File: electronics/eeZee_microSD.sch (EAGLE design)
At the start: 14 parts, among them U1 MCP1824S, U2 74HC4050, U3 USD-SOCKET

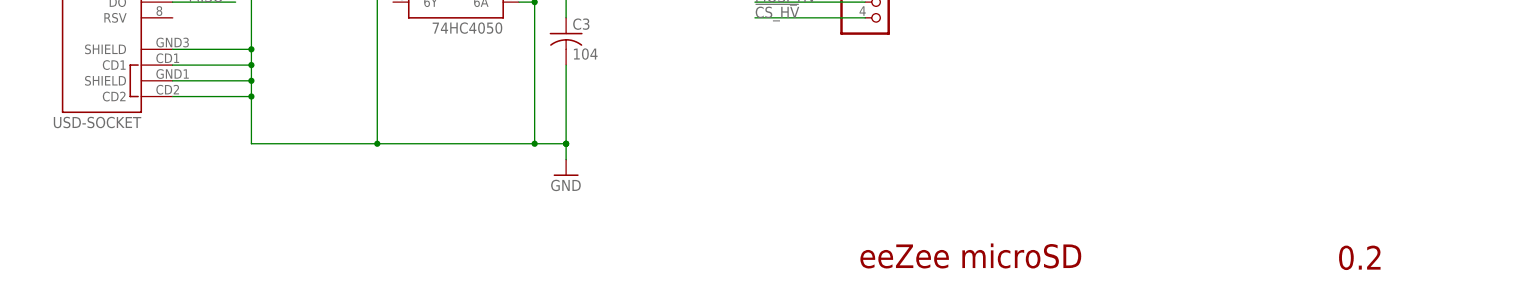
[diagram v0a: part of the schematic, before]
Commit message: Updated schematic version and usd socket value
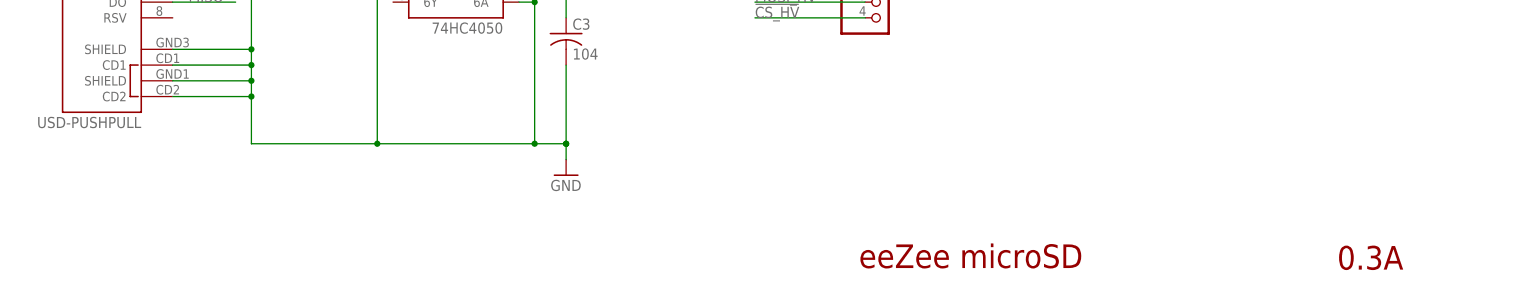
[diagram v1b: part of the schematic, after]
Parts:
- U3: value USD-SOCKET -> USD-PUSHPULL
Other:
- note added: "0.3A"
- note removed: "0.2"
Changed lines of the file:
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@@
 <part name="JP5" library="mes_electromech" deviceset="PINHEAD-2" device="BIG" value="PWR"/>
 <part name="JP4" library="mes_electromech" deviceset="PINHEAD-2" device="BIG" value="PWR"/>
-<part name="U3" library="SparkFun-Connectors" deviceset="USD-SOCKET" device=""/>
+<part name="U3" library="SparkFun-Connectors" deviceset="USD-SOCKET" device="" value="USD-PUSHPULL"/>
 </parts>
 <sheets>
@@
 <text x="181.864" y="143.51" size="1.778" layer="97">to bypass regulator and send VCC direct to the microSD</text>
 <text x="153.924" y="23.114" size="3.81" layer="94">eeZee microSD</text>
-<text x="231.14" y="22.86" size="3.81" layer="94">0.2</text>
+<text x="231.14" y="22.86" size="3.81" layer="94">0.3A</text>
 </plain>
 <instances>

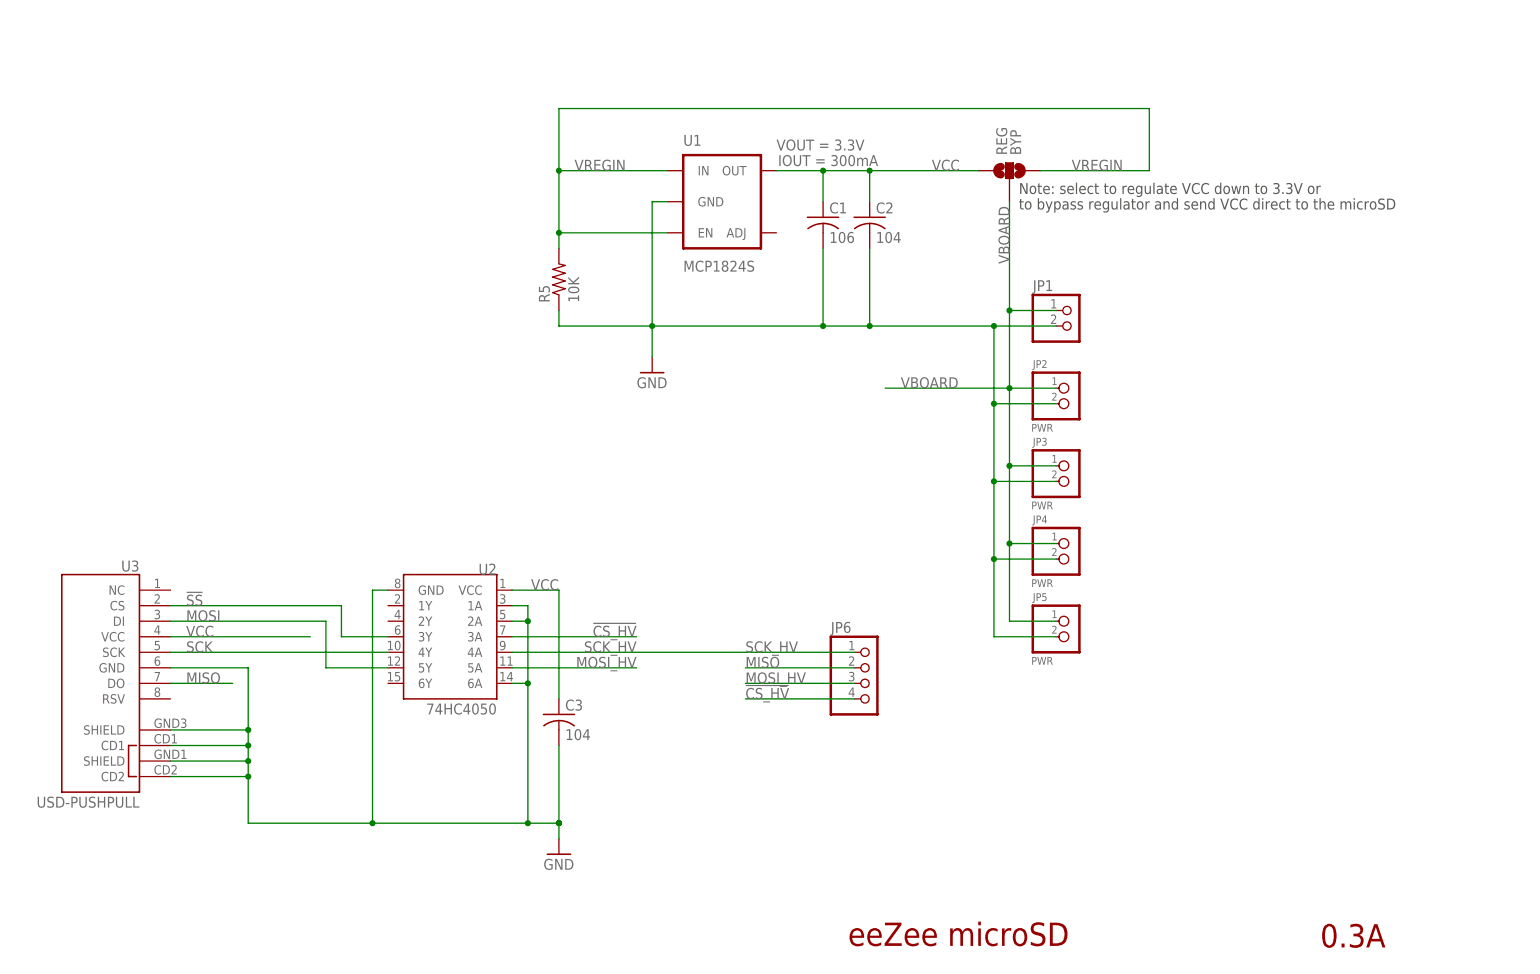
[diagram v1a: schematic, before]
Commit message: Updated version with flip-top socket
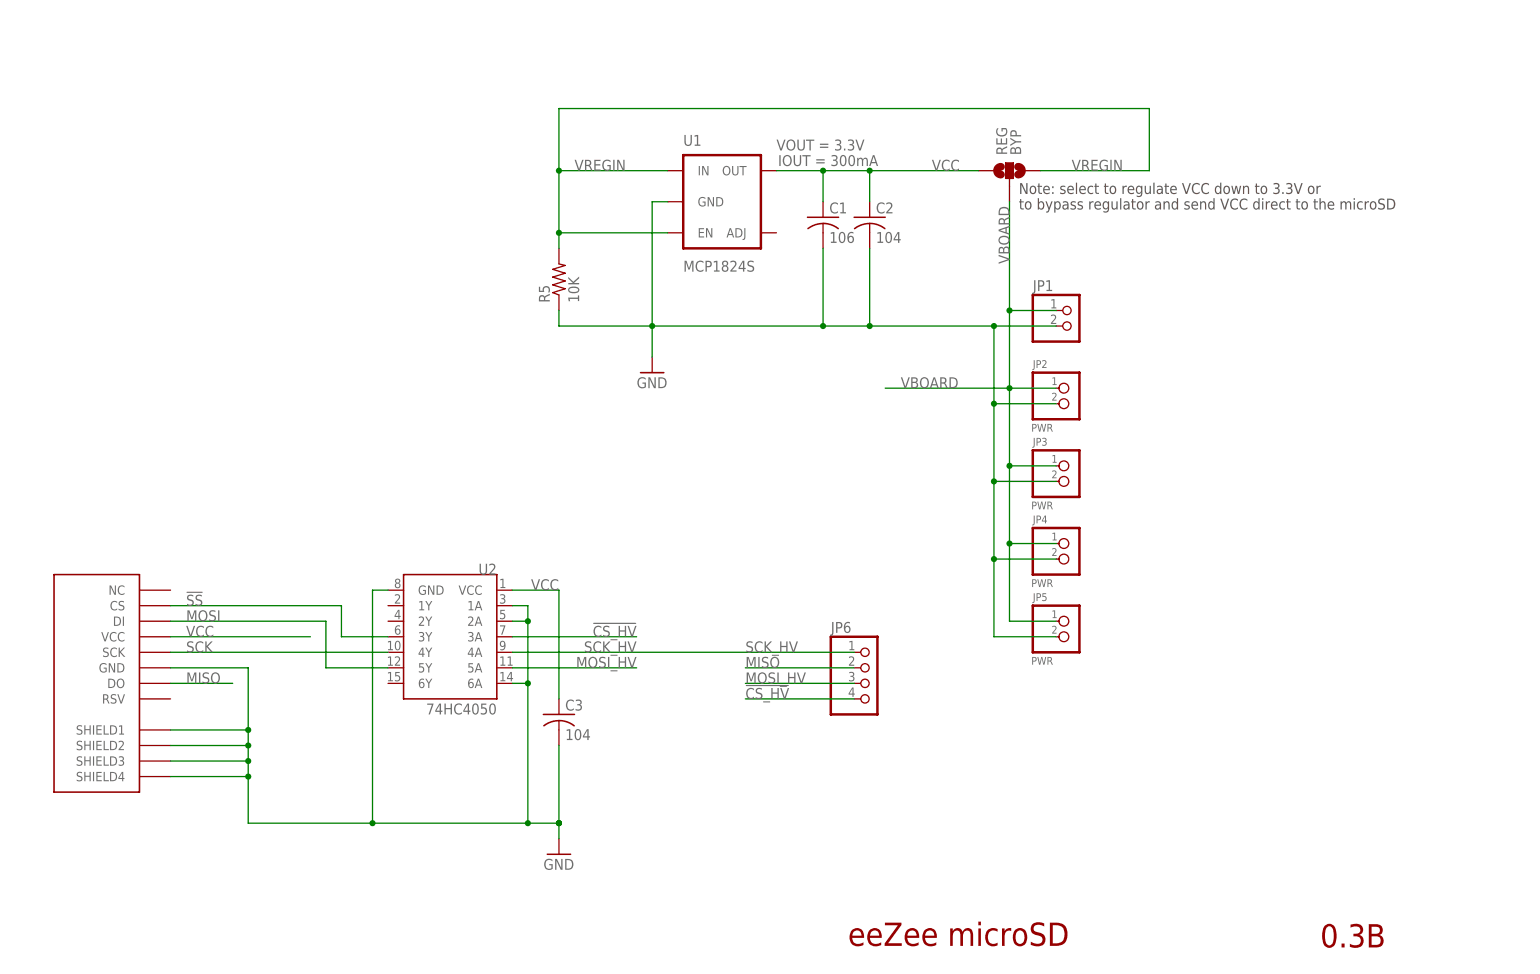
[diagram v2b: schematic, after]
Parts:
- removed U3: USD-PUSHPULL, SparkFun-Connectors:USD-SOCKET
- added U$1: MICROSD_TFLASH, bt_electromech:MICROSD_TFLASH
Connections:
- net !SS: now also U$1.CS; no longer U3.CS
- net GND: now also U$1.GND, U$1.SHIELD1, U$1.SHIELD2, U$1.SHIELD3, U$1.SHIELD4; no longer U3.CD1, U3.CD2, U3.GND, U3.SHIELD@1, U3.SHIELD@3
- net MISO: now also U$1.DO; no longer U3.DO
- net MOSI: now also U$1.DI; no longer U3.DI
- net SCK: now also U$1.SCK; no longer U3.SCK
- net VCC: now also U$1.VCC; no longer U3.VCC
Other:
- note added: "0.3B"
- note removed: "0.3A"
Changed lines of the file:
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@@
 <layer number="49" name="Reference" color="7" fill="1" visible="yes" active="no"/>
 <layer number="50" name="dxf" color="7" fill="1" visible="yes" active="no"/>
-<layer number="51" name="tDocu" color="11" fill="1" visible="yes" active="no"/>
+<layer number="51" name="tDocu" color="15" fill="1" visible="yes" active="no"/>
 <layer number="52" name="bDocu" color="7" fill="1" visible="yes" active="no"/>
 <layer number="53" name="tGND_GNDA" color="7" fill="9" visible="yes" active="no"/>
@@
 <part name="JP5" library="mes_electromech" deviceset="PINHEAD-2" device="BIG" value="PWR"/>
 <part name="JP4" library="mes_electromech" deviceset="PINHEAD-2" device="BIG" value="PWR"/>
-<part name="U3" library="SparkFun-Connectors" deviceset="USD-SOCKET" device="" value="USD-PUSHPULL"/>
+<part name="U$1" library="bt_electromech" deviceset="MICROSD" device="_TFLASH"/>
 </parts>
 <sheets>
@@
 <text x="181.864" y="143.51" size="1.778" layer="97">to bypass regulator and send VCC direct to the microSD</text>
 <text x="153.924" y="23.114" size="3.81" layer="94">eeZee microSD</text>
-<text x="231.14" y="22.86" size="3.81" layer="94">0.3A</text>
+<text x="231.14" y="22.86" size="3.81" layer="94">0.3B</text>
 </plain>
 <instances>
@@
 <instance part="JP5" gate="JP1" x="190.5" y="73.66"/>
 <instance part="JP4" gate="JP1" x="190.5" y="86.36"/>
-<instance part="U3" gate="G$1" x="35.56" y="68.58" rot="MR0"/>
+<instance part="U$1" gate="G$1" x="30.48" y="66.04"/>
 </instances>
 <busses>
@@
 <pinref part="U2" gate="G$1" pin="5Y"/>
 <wire x1="78.74" y1="68.58" x2="68.58" y2="68.58" width="0.1524" layer="91"/>
-<pinref part="U3" gate="G$1" pin="DI"/>
+<pinref part="U$1" gate="G$1" pin="DI"/>
 </segment>
 </net>
@@
 <pinref part="U2" gate="G$1" pin="4Y"/>
 <wire x1="78.74" y1="71.12" x2="43.18" y2="71.12" width="0.1524" layer="91"/>
-<pinref part="U3" gate="G$1" pin="SCK"/>
+<pinref part="U$1" gate="G$1" pin="SCK"/>
 </segment>
 </net>
@@
 <segment>
 <label x="45.72" y="66.04" size="1.778" layer="95"/>
-<pinref part="U3" gate="G$1" pin="DO"/>
 <wire x1="43.18" y1="66.04" x2="53.34" y2="66.04" width="0.1524" layer="91"/>
+<pinref part="U$1" gate="G$1" pin="DO"/>
 </segment>
 <segment>
@@
 <wire x1="78.74" y1="73.66" x2="71.12" y2="73.66" width="0.1524" layer="91"/>
 <wire x1="71.12" y1="73.66" x2="71.12" y2="78.74" width="0.1524" layer="91"/>
-<pinref part="U3" gate="G$1" pin="CS"/>
+<pinref part="U$1" gate="G$1" pin="CS"/>
 </segment>
 </net>
@@
 <junction x="106.68" y="43.18"/>
 <junction x="106.68" y="43.18"/>
-<pinref part="U3" gate="G$1" pin="GND"/>
-<pinref part="U3" gate="G$1" pin="SHIELD@3"/>
-<pinref part="U3" gate="G$1" pin="SHIELD@1"/>
-<pinref part="U3" gate="G$1" pin="CD1"/>
-<pinref part="U3" gate="G$1" pin="CD2"/>
+<pinref part="U$1" gate="G$1" pin="GND"/>
+<pinref part="U$1" gate="G$1" pin="SHIELD1"/>
+<pinref part="U$1" gate="G$1" pin="SHIELD2"/>
+<pinref part="U$1" gate="G$1" pin="SHIELD3"/>
+<pinref part="U$1" gate="G$1" pin="SHIELD4"/>
 </segment>
 <segment>
@@
 <label x="45.72" y="73.66" size="1.778" layer="95"/>
 <wire x1="66.04" y1="73.66" x2="43.18" y2="73.66" width="0.1524" layer="91"/>
-<pinref part="U3" gate="G$1" pin="VCC"/>
-</segment>
-</net>
+<pinref part="U$1" gate="G$1" pin="VCC"/>
+</segment>
+</net>

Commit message: Used small manual connector. Total layout redesign, shrunk board considerably, removed power rail pin headers
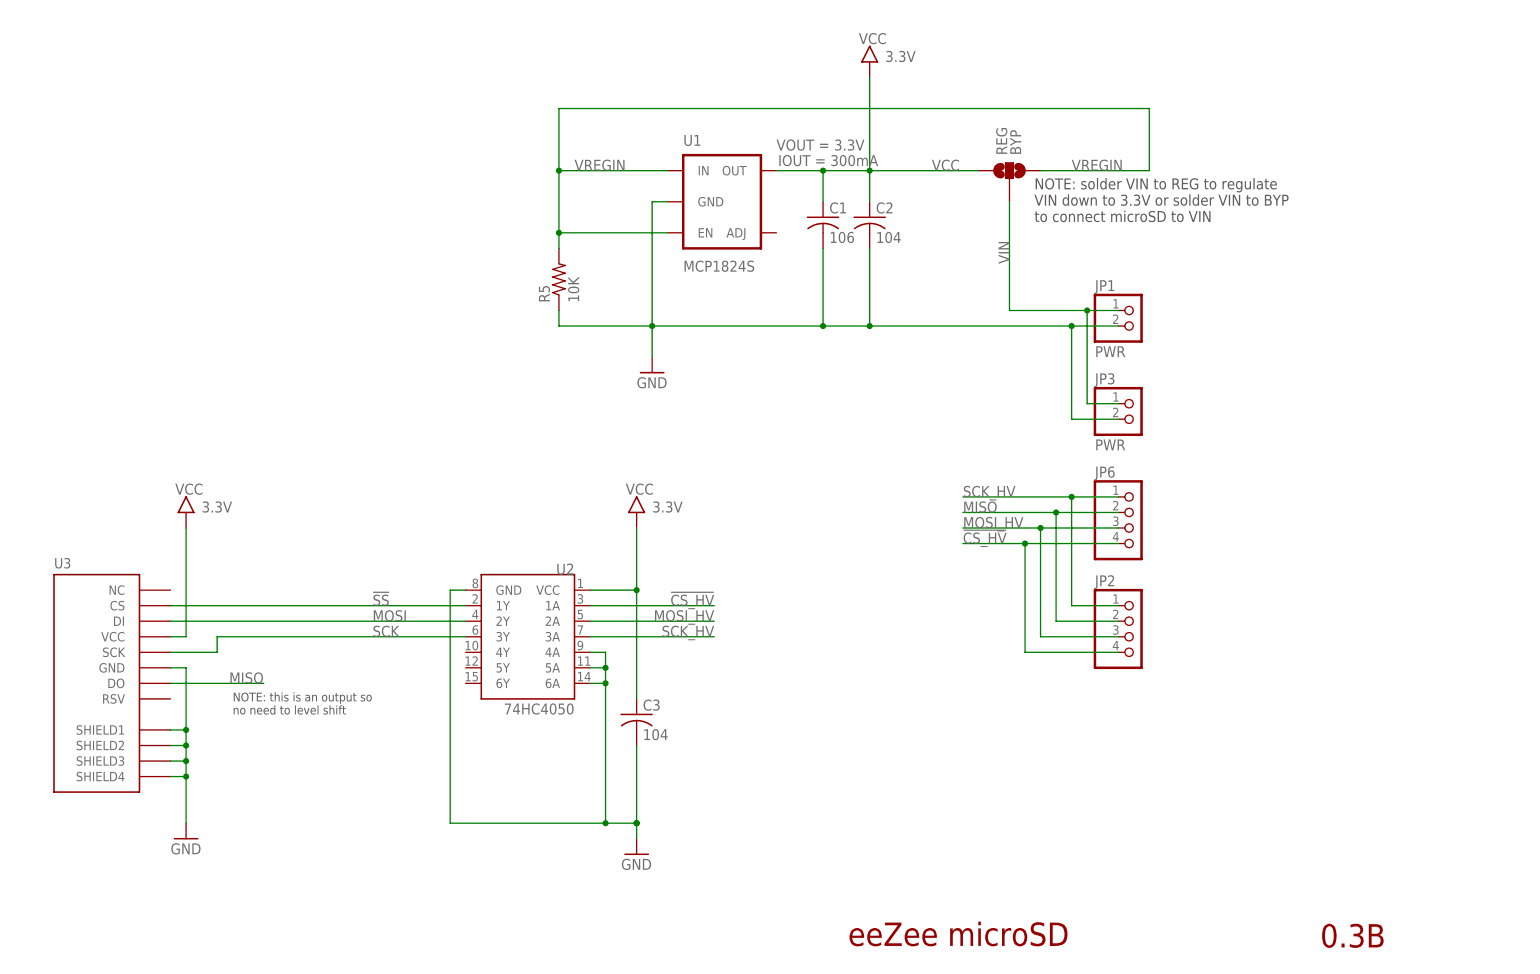
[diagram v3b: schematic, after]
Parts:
- removed JP4, JP5: PWR, mes_electromech:PINHEAD-2BIG
- removed U$1: MICROSD_TFLASH, bt_electromech:MICROSD_TFLASH
- added U3: MICROSD_SMALL, bt_electromech:MICROSD_SMALL
- JP1: value (none) -> PWR
- JP2: value PWR -> (none); device mes_electromech:PINHEAD-2BIG -> pinhead-2:PINHD-1X04_2.54-S
- JP3: device mes_electromech:PINHEAD-2BIG -> pinhead-2:PINHD-1X02_2.54-S
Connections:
- removed net VBOARD: JP1.1, JP2.1, JP3.1, JP4.1, JP5.1, REG.2
- new net VIN: JP1.1, JP3.1, REG.2
- net !CS_HV: now also JP2.4, U2.1A; no longer U2.3A
- net !SS: now also U2.1Y, U3.CS; no longer U$1.CS, U2.3Y
- net GND: now also U2.4A, U2.5A, U3.GND, U3.SHIELD1, U3.SHIELD2, U3.SHIELD3, U3.SHIELD4; no longer JP2.2, JP4.2, JP5.2, U$1.GND, U$1.SHIELD1, U$1.SHIELD2, U$1.SHIELD3, U$1.SHIELD4, U2.1A, U2.2A
- net MISO: now also JP2.2, U3.DO; no longer U$1.DO
- net MOSI: now also U2.2Y, U3.DI; no longer U$1.DI, U2.5Y
- net MOSI_HV: now also JP2.3, U2.2A; no longer U2.5A
- net SCK: now also U2.3Y, U3.SCK; no longer U$1.SCK, U2.4Y
- net SCK_HV: now also JP2.1, U2.3A; no longer U2.4A
- net VCC: now also U3.VCC; no longer U$1.VCC
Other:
- note added: "NOTE: solder VIN to REG to regulate VIN down to 3.3V or solder VIN to BYP to connect microSD to VIN"
- note added: "NOTE: this is an output so no need to level shift"
- note removed: "Note: select to regulate VCC down to 3.3V or"
- note removed: "to bypass regulator and send VCC direct to the microSD"
- moved on the sheet: C3, JP1, JP6, U2

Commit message: Additional layout changes, connected Card Detect
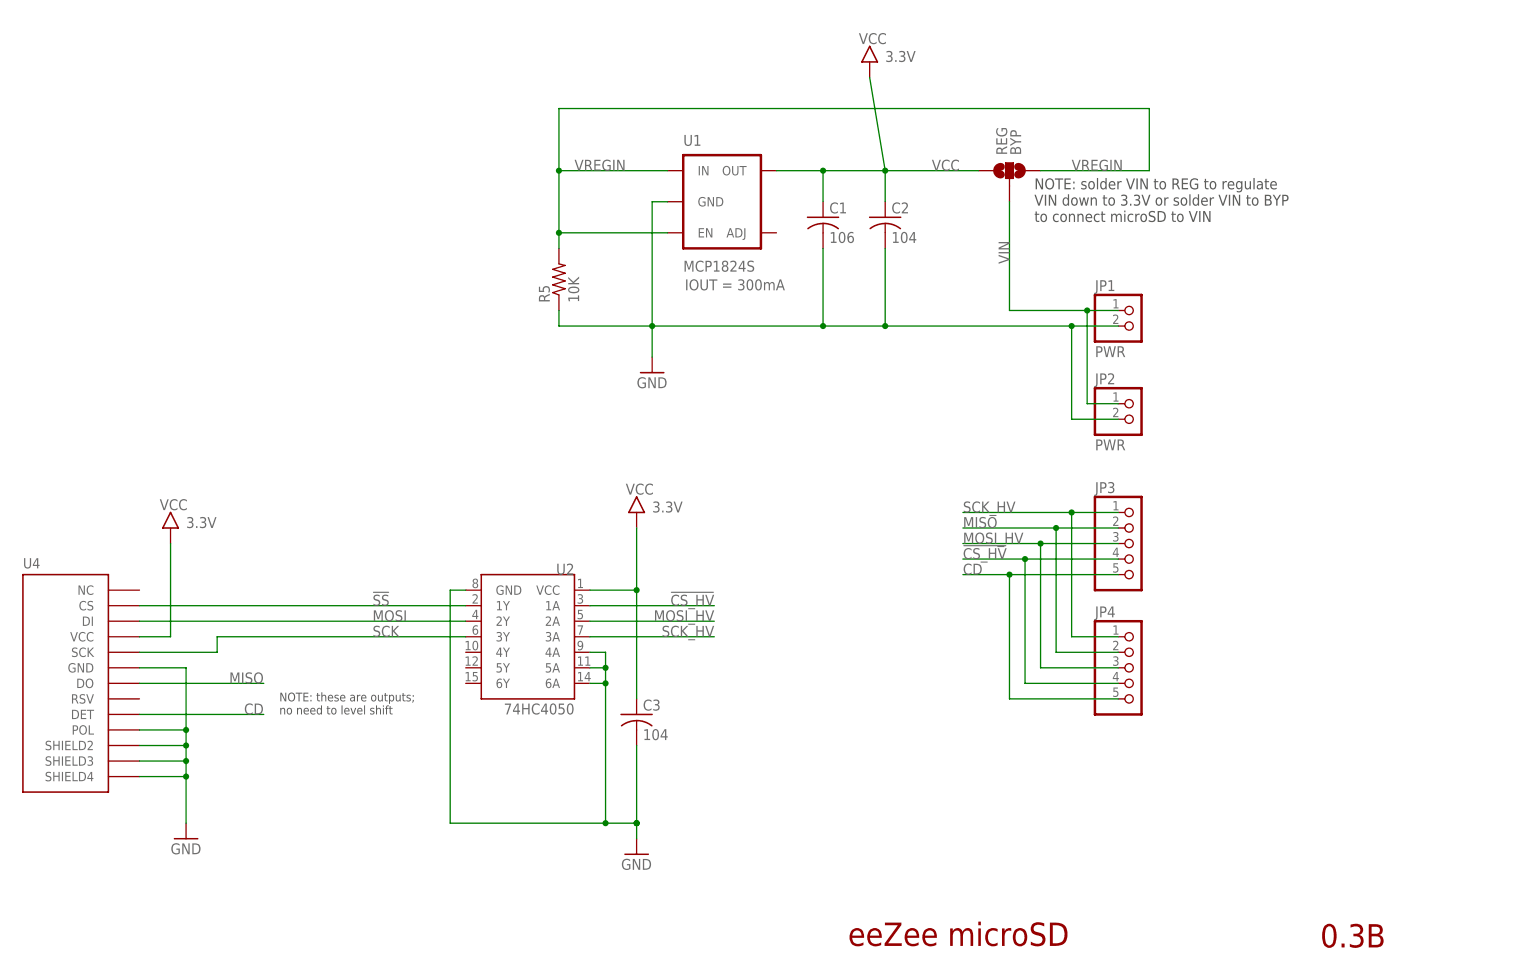
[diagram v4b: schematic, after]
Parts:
- removed JP6: (no value), pinhead-2:PINHD-1X04_2.54-S
- removed U3: MICROSD_SMALL, bt_electromech:MICROSD_SMALL
- added JP4: (no value), pinhead-2:PINHD-1X05_2.54-S
- added U4: MICROSD_CD, bt_electromech:MICROSD_CD
- JP2: value (none) -> PWR; device pinhead-2:PINHD-1X04_2.54-S -> pinhead-2:PINHD-1X02_2.54-S
- JP3: value PWR -> (none); device pinhead-2:PINHD-1X02_2.54-S -> pinhead-2:PINHD-1X05_2.54-S
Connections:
- new net CD: JP3.5, JP4.5, U4.DET
- net !CS_HV: now also JP3.4, JP4.4; no longer JP2.4, JP6.4
- net !SS: now also U4.CS; no longer U3.CS
- net GND: now also JP2.2, U4.GND, U4.POL, U4.SHIELD2, U4.SHIELD3, U4.SHIELD4; no longer JP3.2, U3.GND, U3.SHIELD1, U3.SHIELD2, U3.SHIELD3, U3.SHIELD4
- net MISO: now also JP3.2, JP4.2, U4.DO; no longer JP2.2, JP6.2, U3.DO
- net MOSI: now also U4.DI; no longer U3.DI
- net MOSI_HV: now also JP3.3, JP4.3; no longer JP2.3, JP6.3
- net SCK: now also U4.SCK; no longer U3.SCK
- net SCK_HV: now also JP3.1, JP4.1; no longer JP2.1, JP6.1
- net VCC: now also U4.VCC; no longer U3.VCC
- net VIN: now also JP2.1; no longer JP3.1
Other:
- note added: "NOTE: these are outputs; no need to level shift"
- note removed: "NOTE: this is an output so no need to level shift"
- moved on the sheet: C2
